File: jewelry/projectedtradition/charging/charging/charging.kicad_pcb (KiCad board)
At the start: 2 copper layers, 19 x 19 mm, 0 parts

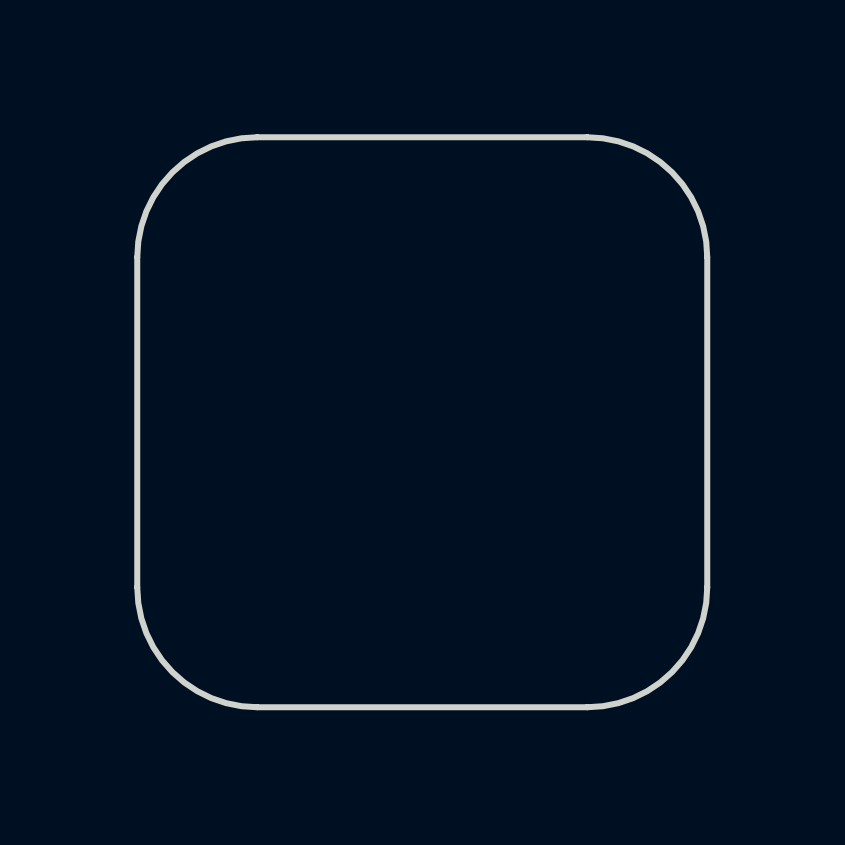
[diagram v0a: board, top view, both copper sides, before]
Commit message: jewelry: Initial layout for charger
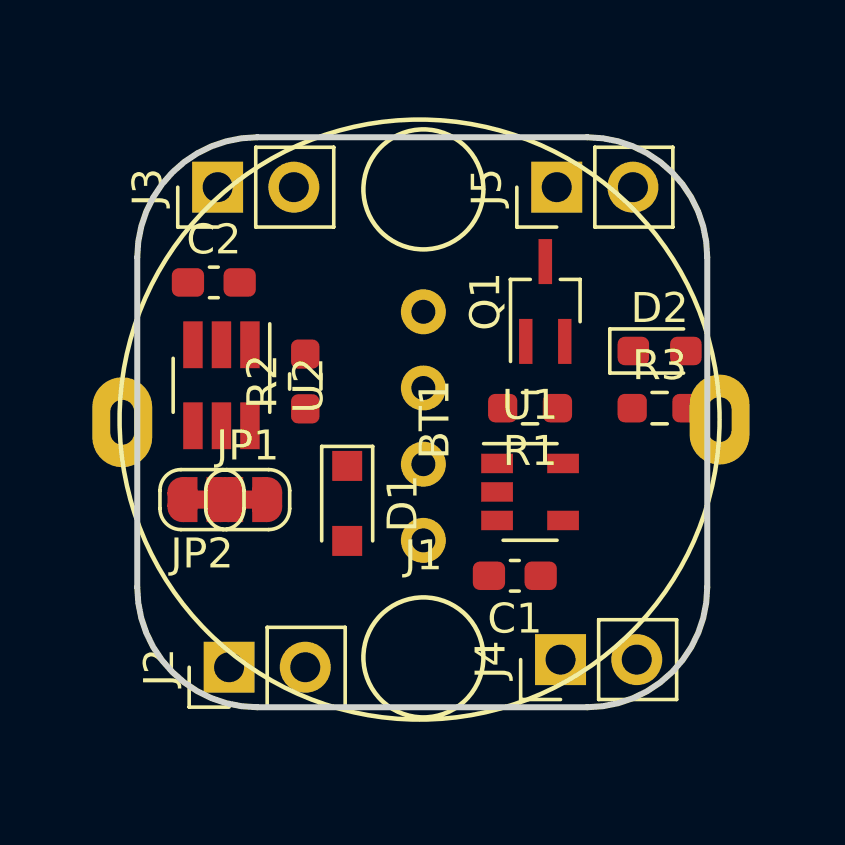
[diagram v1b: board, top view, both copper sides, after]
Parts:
- added BT1: Battery_Cell, charging:batt-lir-2012, F.Cu at (49.9, 49.9)
- added C1: C, Capacitor_SMD:C_0603_1608Metric_Pad1.08x0.95mm_HandSolder, F.Cu at (53.1, 55.1)
- added C2: C, Capacitor_SMD:C_0603_1608Metric_Pad1.08x0.95mm_HandSolder, F.Cu at (43.1, 45.3)
- added D1: D_Schottky, Diode_SMD:D_SOD-323_HandSoldering, F.Cu at (47.5, 52.7)
- added D2: LED, LED_SMD:LED_0603_1608Metric_Pad1.05x0.95mm_HandSolder, F.Cu at (57.9, 47.6)
- added J1: Conn_01x04, charging:magconnect4, F.Cu at (50.0, 50.0)
- added J2: Conn_01x02, Connector_PinHeader_2.54mm:PinHeader_1x02_P2.54mm_Vertical, F.Cu at (43.6, 58.2)
- added J3: Conn_01x02, Connector_PinHeader_2.54mm:PinHeader_1x02_P2.54mm_Vertical, F.Cu at (43.2, 42.2)
- added J4: Conn_01x02, Connector_PinHeader_2.54mm:PinHeader_1x02_P2.54mm_Vertical, F.Cu at (54.6, 57.9)
- added J5: Conn_01x02, Connector_PinHeader_2.54mm:PinHeader_1x02_P2.54mm_Vertical, F.Cu at (54.5, 42.2)
- added JP1: SolderJ, Jumper:SolderJumper-2_P1.3mm_Bridged_RoundedPad1.0x1.5mm, F.Cu at (44.2, 52.6)
- added JP2: SolderJ, Jumper:SolderJumper-2_P1.3mm_Bridged_RoundedPad1.0x1.5mm, F.Cu at (42.7, 52.6)
- added Q1: PMOS SOT223, Package_TO_SOT_SMD:SOT-323_SC-70_Handsoldering, F.Cu at (54.1, 46.0)
- added R1: 22k, Resistor_SMD:R_0603_1608Metric_Pad0.98x0.95mm_HandSolder, F.Cu at (53.6, 49.5)
- added R2: 22k, Resistor_SMD:R_0603_1608Metric_Pad0.98x0.95mm_HandSolder, F.Cu at (46.1, 48.6)
- added R3: 1k2, Resistor_SMD:R_0603_1608Metric_Pad0.98x0.95mm_HandSolder, F.Cu at (57.9, 49.5)
- added U1: MCP73812T-420I-OT, Package_TO_SOT_SMD:SOT-23-5, F.Cu at (53.6, 52.3)
- added U2: TPP223-BA6, Package_TO_SOT_SMD:SOT-23-6_Handsoldering, F.Cu at (43.3, 48.8)

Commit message: jewelry: More compact charging design
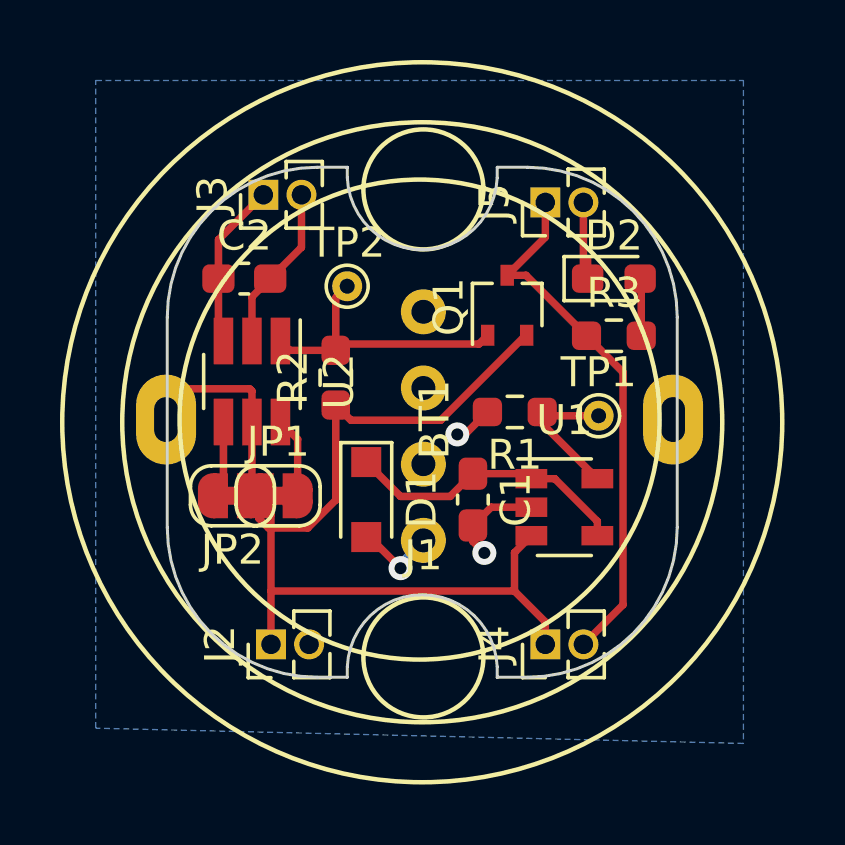
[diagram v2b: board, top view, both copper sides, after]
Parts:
- added TP1: TestPoint, TestPoint:TestPoint_THTPad_D1.0mm_Drill0.5mm, F.Cu at (55.9, 49.8)
- added TP2: TestPoint, TestPoint:TestPoint_THTPad_D1.0mm_Drill0.5mm, F.Cu at (47.5, 45.5)
- J2, J3, J4, J5: footprint Connector_PinHeader_2.54mm:PinHeader_1x02_P2.54mm_Vertical -> Connector_PinHeader_1.27mm:PinHeader_1x02_P1.27mm_Vertical
- Q1: footprint Package_TO_SOT_SMD:SOT-323_SC-70_Handsoldering -> Package_TO_SOT_SMD:SOT-323_SC-70
- moved C1 2.90 mm to (51.7, 52.6), turned to 270 degrees
- moved R3 2.85 mm to (56.4, 47.1)
- moved D2 2.85 mm to (56.4, 45.2)
- moved J2 1.59 mm to (45.0, 57.4)
- moved J3 1.55 mm to (44.7, 42.4)
- moved Q1 1.28 mm to (52.8, 46.1)
- moved U1 1.25 mm to (54.7, 52.8)
- moved JP1 1.02 mm to (45.2, 52.5)
- moved JP2 1.02 mm to (43.7, 52.5)
- moved C2 1.02 mm to (44.1, 45.2)
- moved U2 1.02 mm to (44.3, 48.6)
- moved R2 1.02 mm to (47.1, 48.5)
- moved J4 0.72 mm to (54.1, 57.4)
- moved D1 0.65 mm to (48.1, 52.6)
- moved J5 0.63 mm to (54.1, 42.7)
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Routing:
- net +BATT: track 0.00 -> 38.4 mm
- net /POWER_OUT: track 0.00 -> 18.0 mm
- net -BATT: track 0.00 -> 13.6 mm, vias 0 -> 2
- net VBUS: track 0.00 -> 9.63 mm
- net /POWER_EN: track 0.00 -> 9.54 mm
- net /TOUCH_SENSE: track 0.00 -> 5.98 mm
- net Net-(R1-Pad1): track 0.00 -> 4.92 mm
- net Net-(D1-Pad2): track 0.00 -> 2.81 mm, vias 0 -> 1
- net Net-(JP1-Pad2): track 0.00 -> 2.70 mm
- net Net-(JP2-Pad2): track 0.00 -> 2.60 mm
- net Net-(D2-Pad2): track 0.00 -> 1.92 mm
- added copper zone on B.Cu, net -BATT
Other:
- board size 19 x 19 mm -> 17 x 17 mm

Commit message: jewelery: Finish a version with charger
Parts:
- J2, J3, J4, J5: footprint Connector_PinHeader_1.27mm:PinHeader_1x02_P1.27mm_Vertical -> charging:PinHeader_1x02_P1.27mm_Vertical
- moved J3 0.25 mm to (44.7, 42.7)
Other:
- outline, holes or cut-outs redrawn
- rule pad_to_mask_clearance: 0.051 -> 0

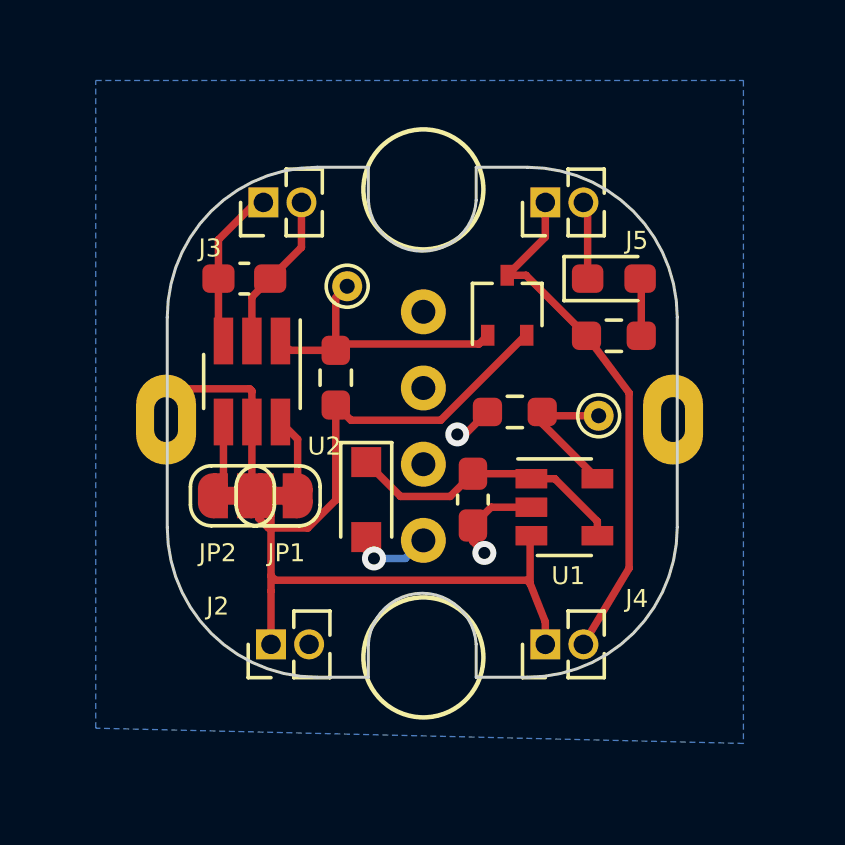
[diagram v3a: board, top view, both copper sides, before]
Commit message: jewelry: Try to design in board2board connecto
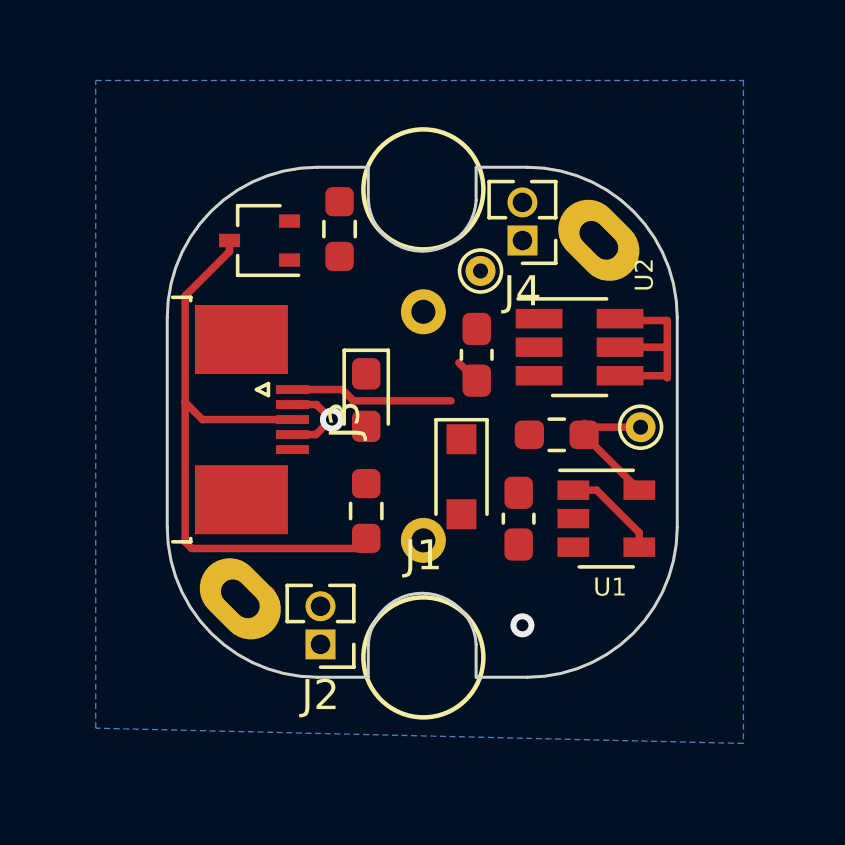
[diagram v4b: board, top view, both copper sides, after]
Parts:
- removed J5: Conn_01x02, charging:PinHeader_1x02_P1.27mm_Vertical
- removed JP1, JP2: SolderJ, Jumper:SolderJumper-2_P1.3mm_Bridged_RoundedPad1.0x1.5mm
- J1: footprint charging:magconnect4 -> charging:magconnect4-poweronly
- J2, J4: footprint charging:PinHeader_1x02_P1.27mm_Vertical -> Connector_PinHeader_1.27mm:PinHeader_1x02_P1.27mm_Vertical
- J3: value Conn_01x02 -> Conn_01x04; footprint charging:PinHeader_1x02_P1.27mm_Vertical -> Connector_FFC-FPC:TE_0-1734839-5_1x05-1MP_P0.5mm_Horizontal
- moved J4 13.5 mm to (53.3, 43.9), turned to 180 degrees
- moved U2 11.0 mm to (55.2, 47.5), turned to 0 degrees
- moved R3 10.1 mm to (48.1, 53.0), turned to 90 degrees
- moved D2 9.19 mm to (48.1, 49.3), turned to 270 degrees
- moved Q1 8.53 mm to (44.6, 43.9), turned to 180 degrees
- moved C2 8.15 mm to (51.8, 47.8), turned to 90 degrees
- moved J3 7.25 mm to (44.3, 49.9), turned to 270 degrees
- moved R2 4.95 mm to (47.2, 43.6), turned to 270 degrees
- moved TP2 4.47 mm to (51.9, 45.0), turned to 90 degrees
- moved D1 3.27 mm to (51.3, 51.8)
- moved J2 1.65 mm to (46.6, 57.4), turned to 180 degrees
- moved C1 1.65 mm to (53.2, 53.2)
- moved R1 1.59 mm to (54.5, 50.4)
- moved TP1 1.45 mm to (57.3, 50.2)
- moved U1 1.45 mm to (56.1, 53.2)
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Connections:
- U2 pad 4: Net-(JP2-Pad2) -> +BATT
- U2 pad 6: Net-(JP1-Pad2) -> +BATT
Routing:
- net +BATT: track 38.5 -> 6.73 mm
- net -BATT: track 13.1 -> 3.09 mm
- net /POWER_EN: track 9.54 -> 0.00 mm
- net VBUS: track 9.63 -> 3.50 mm
- net /POWER_OUT: track 17.9 -> 20.7 mm
- net Net-(D1-Pad2): track 2.72 -> 0.00 mm, vias 1 -> 0
- net Net-(JP1-Pad2): track 2.70 -> 0.00 mm
- net Net-(JP2-Pad2): track 2.60 -> 0.00 mm
- net Net-(D2-Pad2): track 1.92 -> 0.00 mm
